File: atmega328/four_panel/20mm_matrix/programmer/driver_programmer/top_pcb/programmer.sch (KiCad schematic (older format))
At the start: 21 parts, among them P1 CONN_3X2, P10 CONN_2, P11 CONN_6, P12 CONN_2, P13 CONN_6, P2 CONN_3X2, P3 CONN_3X2, P4 CONN_3X2, P5 CONN_3X2, P6 CONN_2, P7 CONN_6, P8 CONN_2, P9 CONN_6

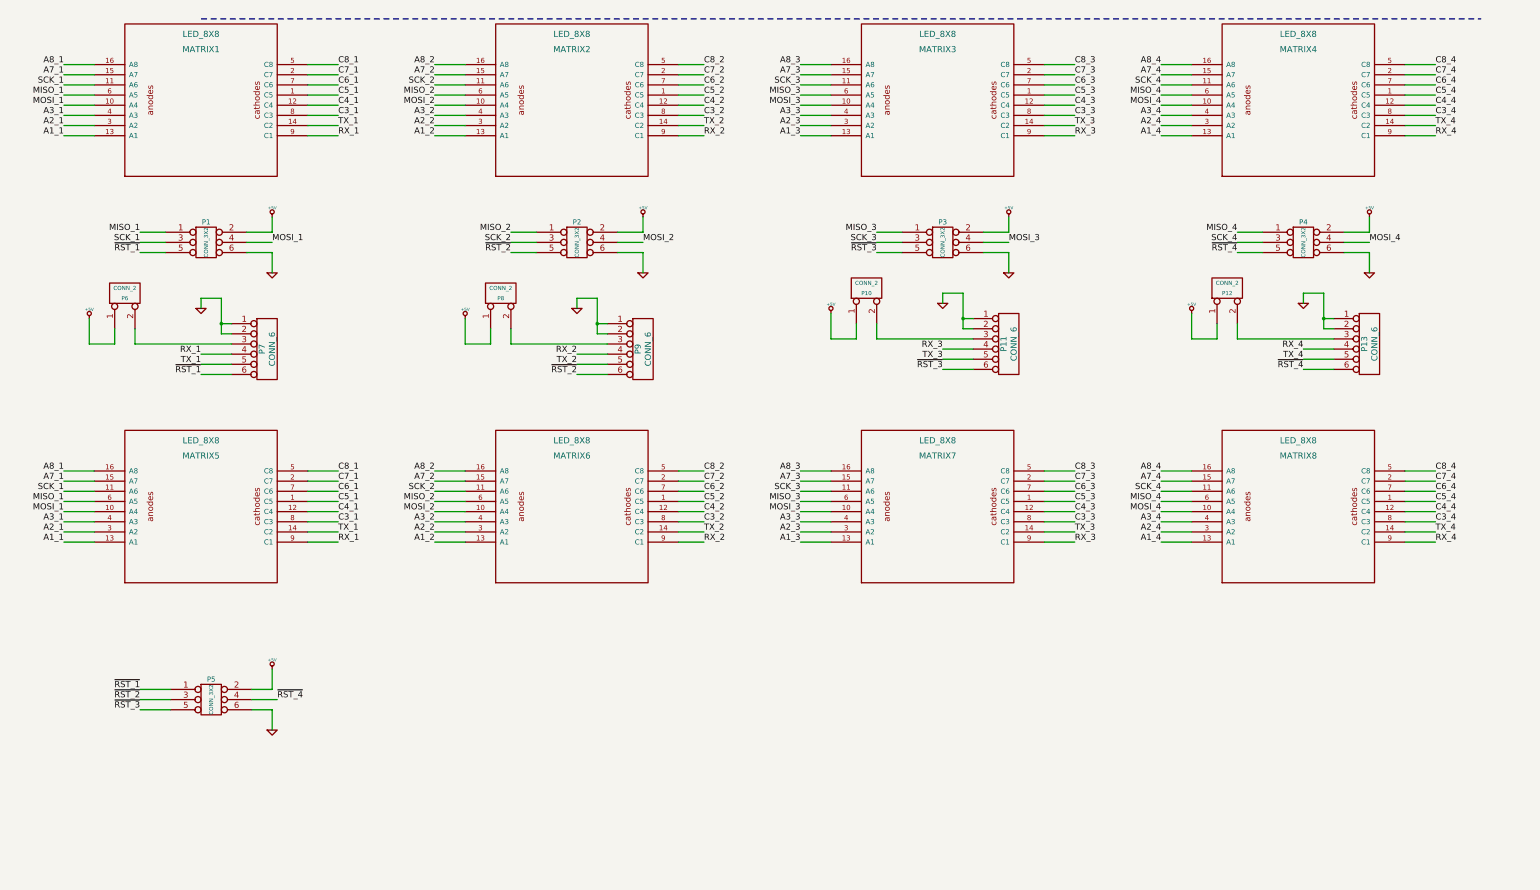
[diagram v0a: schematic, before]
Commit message: Fixed minor issues with test arenas and programmer pcbs.
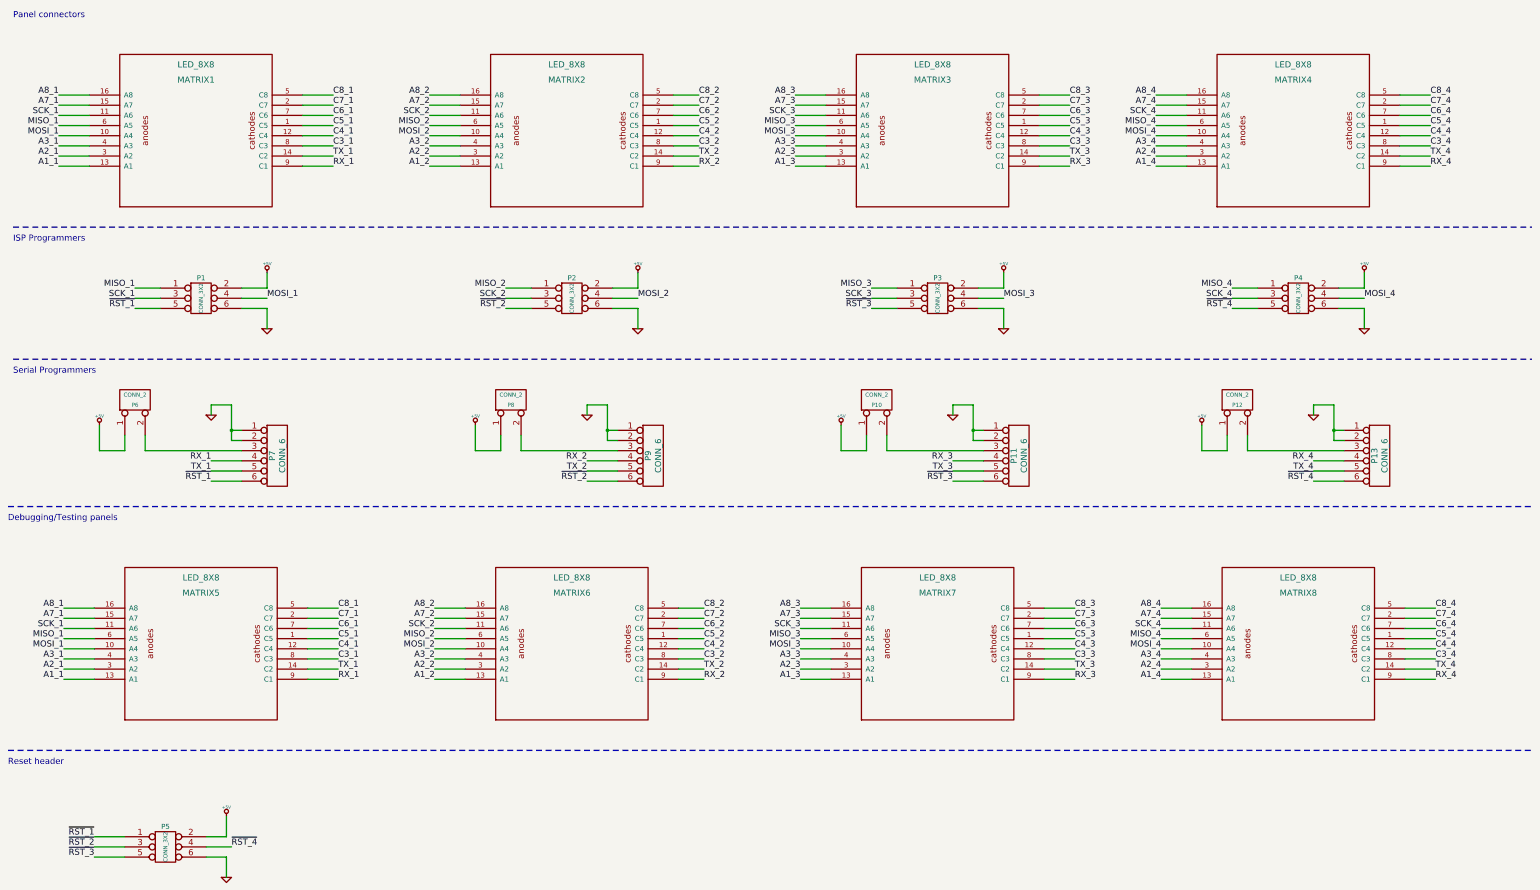
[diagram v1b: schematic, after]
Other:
- note added: "Debugging/Testing panels"
- note added: "ISP Programmers"
- note added: "Panel connectors"
- note added: "Reset header"
- note added: "Serial Programmers"
- moved on the sheet: MATRIX1, MATRIX2, MATRIX3, MATRIX4, MATRIX5, MATRIX6, MATRIX7, MATRIX8, P1, P10, P11, P12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

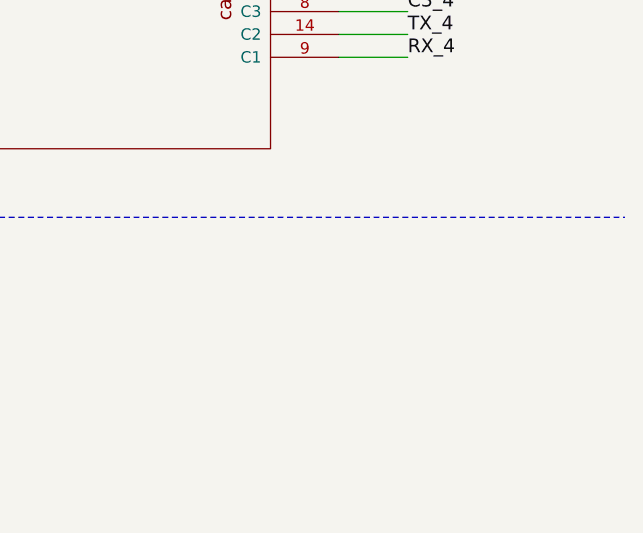
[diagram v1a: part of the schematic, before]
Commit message: Created gerber files for test_arena and programmer pcbs. Fixed of few small errors.
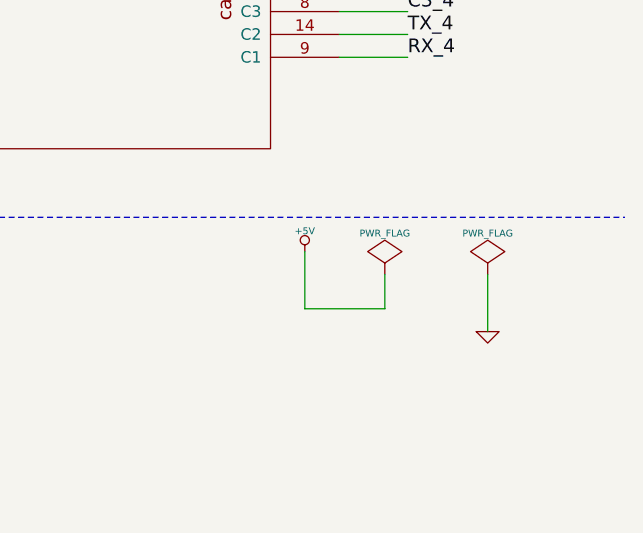
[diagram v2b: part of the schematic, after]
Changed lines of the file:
@@
 Text Notes 500  8100 0    60   ~ 0
 Reset header
+$Comp
+L +5V #PWR019
+U 1 1 5282D5E6
+P 14100 8100
+F 0 "#PWR019" H 14100 8190 20  0001 C CNN
+F 1 "+5V" H 14100 8190 30  0000 C CNN
+F 2 "" H 14100 8100 60  0000 C CNN
+F 3 "" H 14100 8100 60  0000 C CNN
+	1    14100 8100
+	1    0    0    -1
+$EndComp
+$Comp
+L GND #PWR020
+U 1 1 5282D5F5
+P 14900 8450
+F 0 "#PWR020" H 14900 8450 30  0001 C CNN
+F 1 "GND" H 14900 8380 30  0001 C CNN
+F 2 "" H 14900 8450 60  0000 C CNN
+F 3 "" H 14900 8450 60  0000 C CNN
+	1    14900 8450
+	1    0    0    -1
+$EndComp
+$Comp
+L PWR_FLAG #FLG021
+U 1 1 5282D60E
+P 14900 8200
+F 0 "#FLG021" H 14900 8295 30  0001 C CNN
+F 1 "PWR_FLAG" H 14900 8380 30  0000 C CNN
+F 2 "" H 14900 8200 60  0000 C CNN
+F 3 "" H 14900 8200 60  0000 C CNN
+	1    14900 8200
+	1    0    0    -1
+$EndComp
+$Comp
+L PWR_FLAG #FLG022
+U 1 1 5282D61D
+P 14450 8200
+F 0 "#FLG022" H 14450 8295 30  0001 C CNN
+F 1 "PWR_FLAG" H 14450 8380 30  0000 C CNN
+F 2 "" H 14450 8200 60  0000 C CNN
+F 3 "" H 14450 8200 60  0000 C CNN
+	1    14450 8200
+	1    0    0    -1
+$EndComp
+Wire Wire Line
+	14100 8100 14100 8350
+Wire Wire Line
+	14100 8350 14450 8350
+Wire Wire Line
+	14450 8350 14450 8200
+Wire Wire Line
+	14900 8200 14900 8450
 $EndSCHEMATC
